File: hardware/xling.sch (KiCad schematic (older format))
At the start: 54 parts, among them J4 USB_OTG, J5 AVR ISP, J6 Battery, Q1 NTR0202PL, Q2 NTR0202PL, Q3 NTA4153N, SW2 BTN, SW3 BTN, SW4 BTN, U1 LT1109CZ-12, U2 ATMEGA328P-AU, U3 DEP_128064I, U4 MCP73831, U5 AP3401_TSOT26, Y1 8MHz

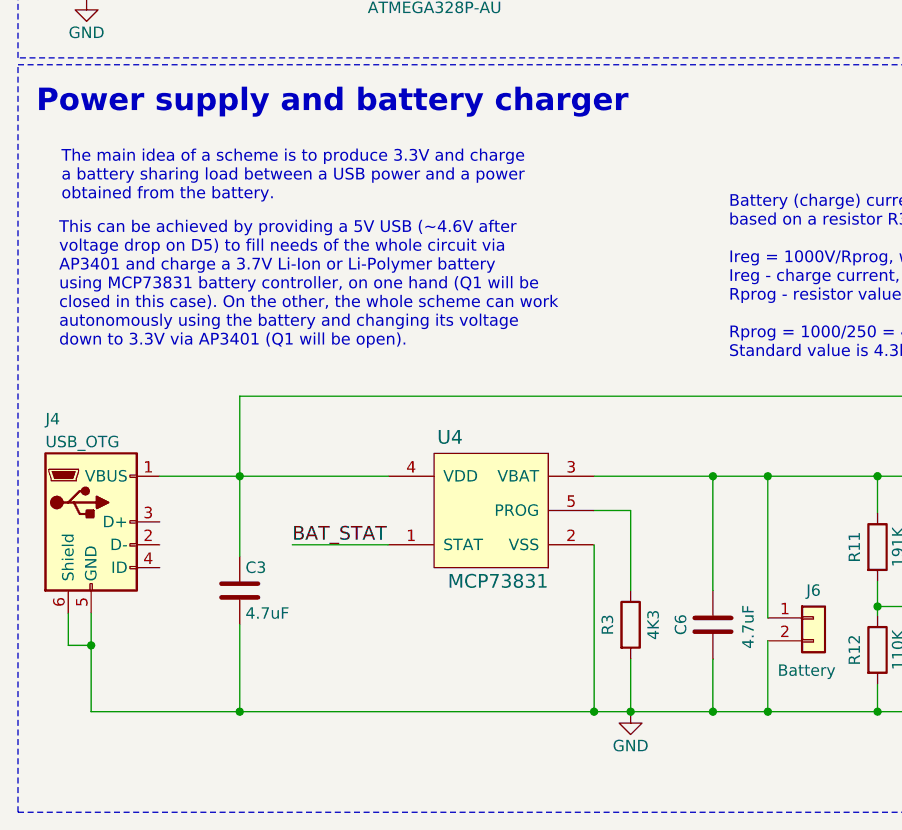
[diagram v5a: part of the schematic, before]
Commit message: patch 0.2.0001: Adjust some footprints.
Several footprints were updated to use rounded rectangles instead of
rectangles with sharp corners as pads.

BOM generator script updated to include a revision into a BOM html file.
It is useful to understand which components are required for a specific
version of the device.

There is a new TSOT26 footprint created and added especially for AP3401
DC-DC converter.

Signed-off-by: Dmitry Salychev <darkness.bsd@gmail.com>
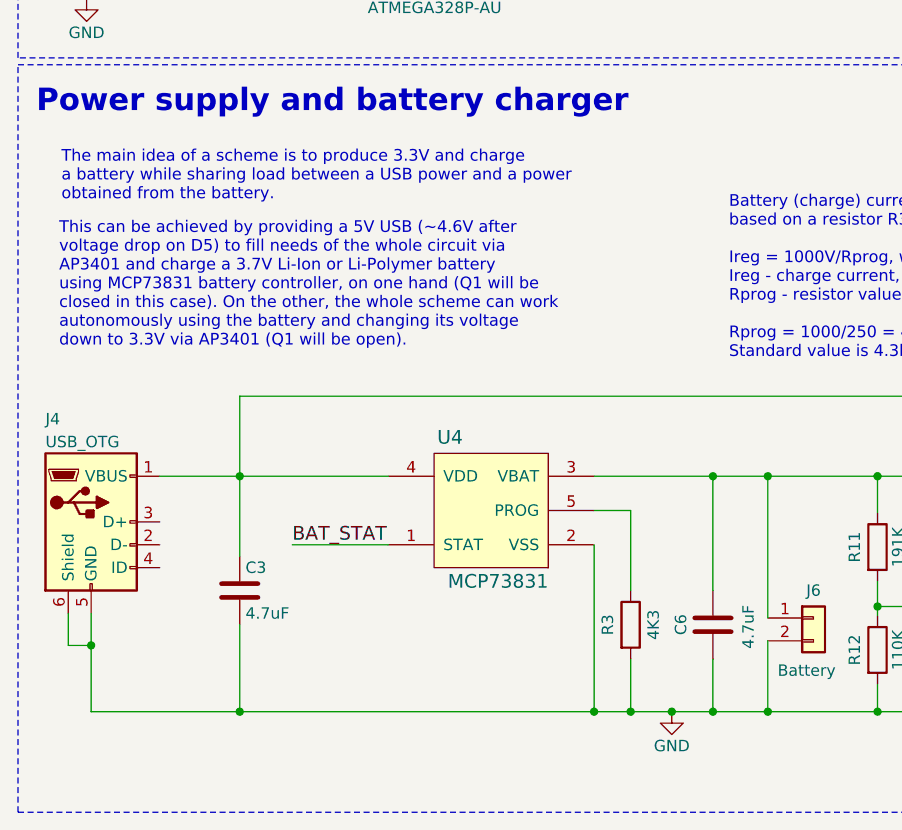
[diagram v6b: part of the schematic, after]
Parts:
- J6: footprint Xling Footprints:Pin_Header_Straight_1x02 -> Xling Footprints:PinHeader_1x02_P2.54mm_Horizontal; Model None -> DS1022-1*20RDF1-1
- U5: footprint (none) -> Xling Footprints:AP3401_TSOT26
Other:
- note added: "The main idea of a scheme is to produce 3.3V and charge\na battery while sharing load between a USB power and a power\nobtained from the battery."
- note removed: "The main idea of a scheme is to produce 3.3V and charge\na battery sharing load between a USB power and a power\nobtained from the battery."
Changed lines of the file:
@@
 Sheet 1 1
 Title "Xling Schematic"
-Date "2018-08-28"
-Rev "0.2.0"
+Date "2018-11-02"
+Rev "0.2.0001"
 Comp "MCUSim"
 Comment1 ""
@@
 L xling:GND #PWR01
 U 1 1 59FC89D1
-P 3390 7810
-F 0 "#PWR01" H 3390 7560 50  0001 C CNN
-F 1 "GND" H 3390 7660 50  0000 C CNN
-F 2 "" H 3390 7810 50  0001 C CNN
-F 3 "" H 3390 7810 50  0001 C CNN
-	1    3390 7810
+P 3570 7810
+F 0 "#PWR01" H 3570 7560 50  0001 C CNN
+F 1 "GND" H 3570 7660 50  0000 C CNN
+F 2 "" H 3570 7810 50  0001 C CNN
+F 3 "" H 3570 7810 50  0001 C CNN
+	1    3570 7810
 	1    0    0    -1
 $EndComp
@@
 F 0 "J6" H 4190 7520 50  0000 C CNN
 F 1 "Battery" H 4160 7170 50  0000 C CNN
-F 2 "Xling Footprints:Pin_Header_Straight_1x02" H 4190 7400 50  0001 C CNN
+F 2 "Xling Footprints:PinHeader_1x02_P2.54mm_Horizontal" H 4190 7400 50  0001 C CNN
 F 3 "" H 4190 7400 50  0001 C CNN
-F 4 "None" H 4190 7400 60  0001 C CNN "Model"
+F 4 "DS1022-1*20RDF1-1" H 4190 7400 60  0001 C CNN "Model"
 	1    4190 7400
 	1    0    0    -1
@@
 F 0 "U5" H 6280 7450 60  0000 C CNN
 F 1 "AP3401_TSOT26" H 6480 6610 60  0000 C CNN
-F 2 "" H 6480 7030 60  0001 C CNN
+F 2 "Xling Footprints:AP3401_TSOT26" H 6480 7030 60  0001 C CNN
 F 3 "" H 6480 7030 60  0001 C CNN
 F 4 "AP3401KTTR-G1" H 6480 7030 50  0001 C CNN "Model"
@@
 Connection ~ 4290 3770
 Text Notes 900  5580 0    51   ~ 0
-The main idea of a scheme is to produce 3.3V and charge\na battery sharing load between a USB power and a power\nobtained from the battery.
+The main idea of a scheme is to produce 3.3V and charge\na battery while sharing load between a USB power and a power\nobtained from the battery.
 Wire Wire Line
 	6930 6980 7000 6980
@@
 	3230 6780 3750 6780
 Wire Wire Line
-	3390 7810 3750 7810
+	3390 7810 3570 7810
 Wire Wire Line
 	3750 7580 3750 7810
@@
 Wire Wire Line
 	3385 1595 2755 1595
+Connection ~ 3570 7810
+Wire Wire Line
+	3570 7810 3750 7810
 $EndSCHEMATC
